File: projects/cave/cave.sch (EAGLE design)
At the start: 113 parts, among them U1 IRLML6344TRPBF, U10 IRLML6344TRPBF, U11 IRLML6344TRPBF, U12 IRLML6344TRPBF, U2 TLC555CDR, U3 IRLML6344TRPBF, U4 IRLML6344TRPBF, U5 IRLML6344TRPBF, U6 IRLML6344TRPBF, U7 TPS54625, U9 IRLML6344TRPBF

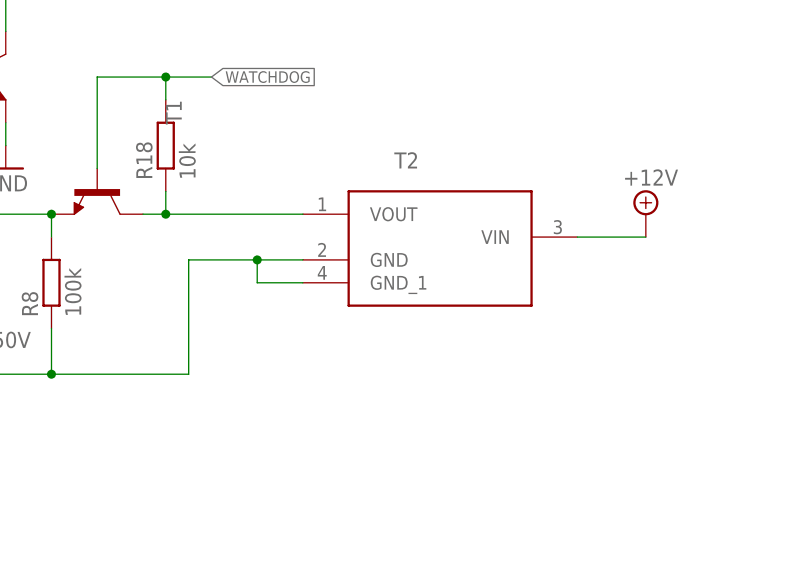
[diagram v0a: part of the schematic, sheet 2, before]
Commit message: Board dimension reduced to 99x70mm (Seeed's limitations). Gerber revA generated
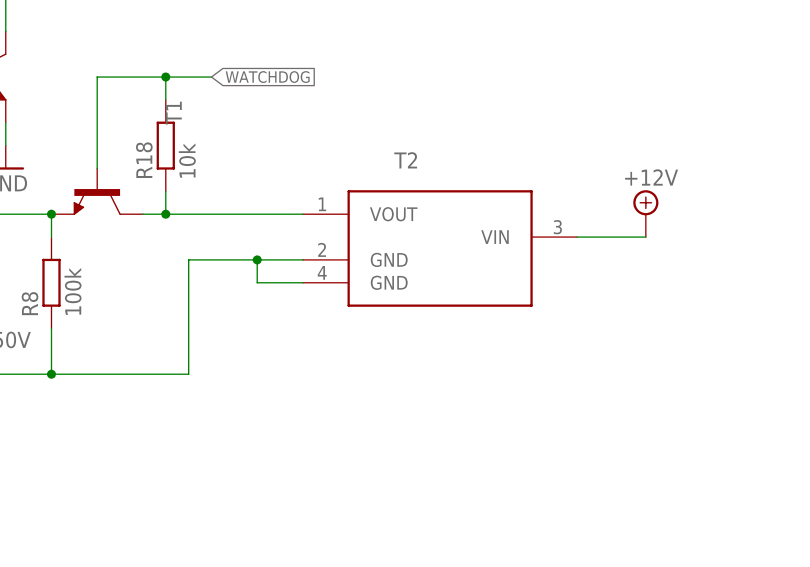
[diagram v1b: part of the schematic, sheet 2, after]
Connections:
- net GND: now also T2.GND@1, T2.GND@2; no longer T2.GND, T2.GND_1
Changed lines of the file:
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@@
 <wire x1="139.7" y1="-25.4" x2="121.92" y2="-25.4" width="0.1524" layer="91"/>
 <junction x="121.92" y="-25.4"/>
-<pinref part="T2" gate="A" pin="GND"/>
+<pinref part="T2" gate="A" pin="GND@1"/>
 <wire x1="167.64" y1="-12.7" x2="162.56" y2="-12.7" width="0.1524" layer="91"/>
 <wire x1="162.56" y1="-12.7" x2="154.94" y2="-12.7" width="0.1524" layer="91"/>
@@
 <wire x1="154.94" y1="-25.4" x2="139.7" y2="-25.4" width="0.1524" layer="91"/>
 <junction x="139.7" y="-25.4"/>
-<pinref part="T2" gate="A" pin="GND_1"/>
+<pinref part="T2" gate="A" pin="GND@2"/>
 <wire x1="167.64" y1="-15.24" x2="162.56" y2="-15.24" width="0.1524" layer="91"/>
 <wire x1="162.56" y1="-15.24" x2="162.56" y2="-12.7" width="0.1524" layer="91"/>

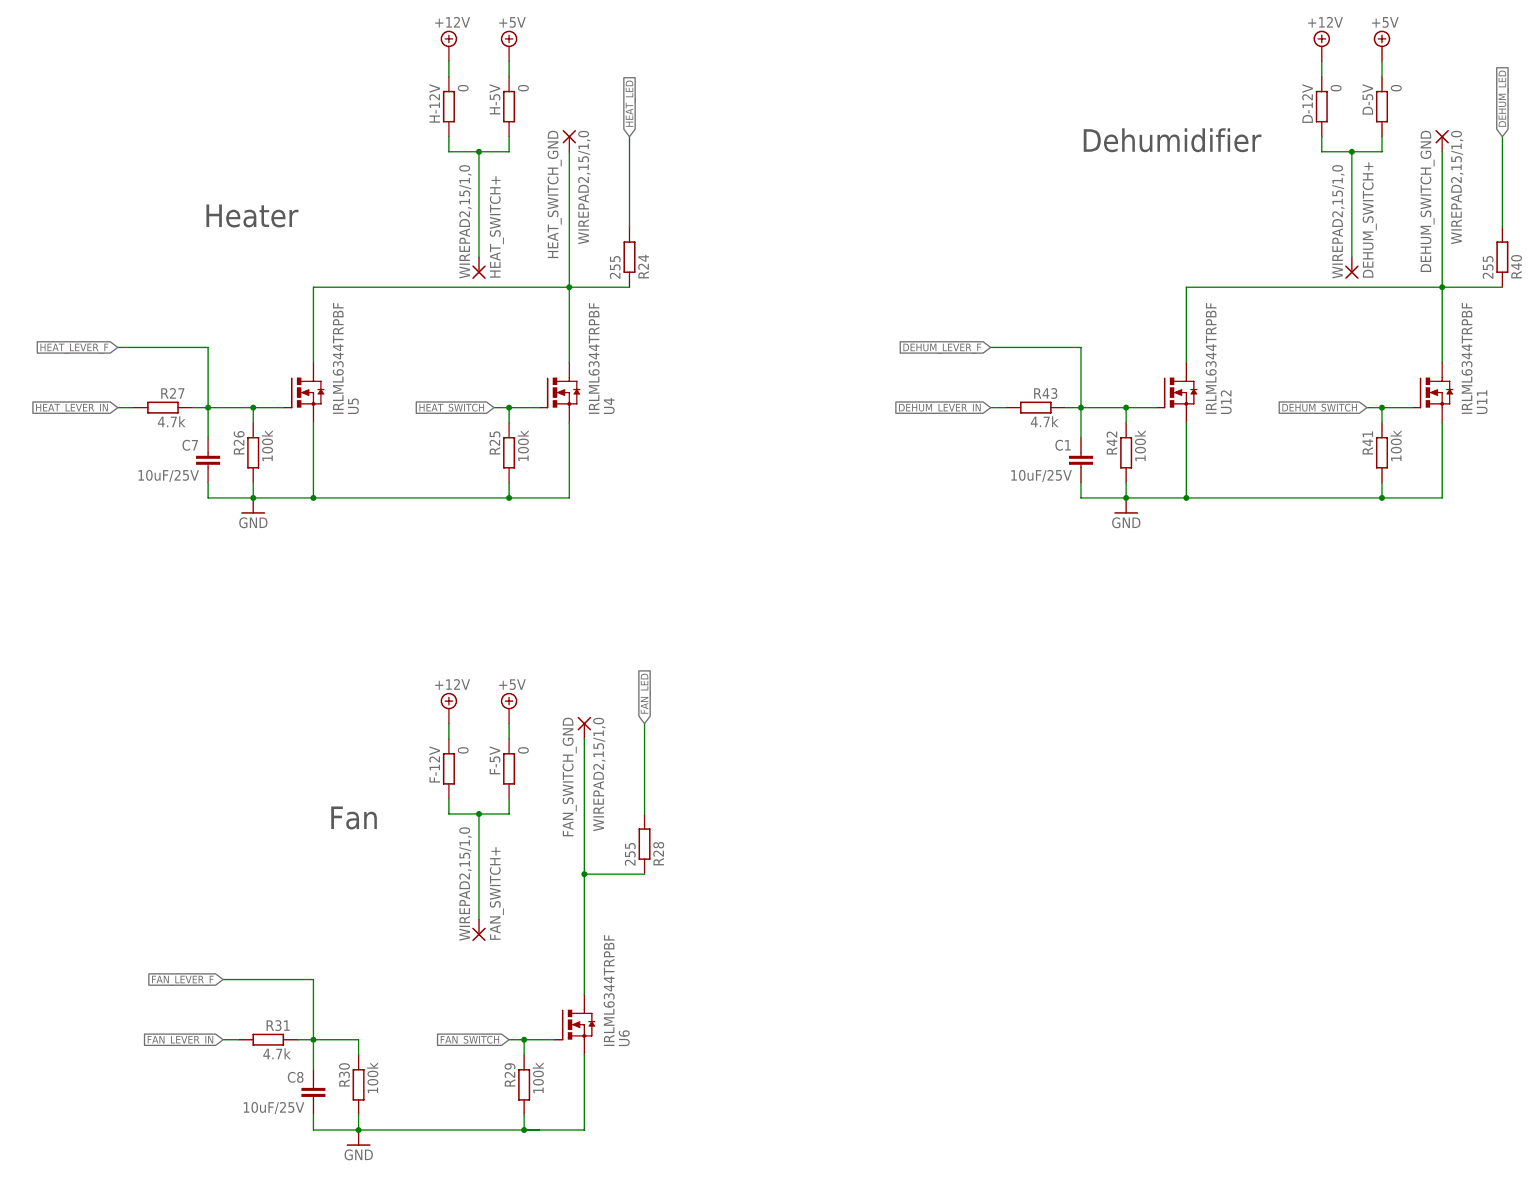
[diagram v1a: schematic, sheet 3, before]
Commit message: Added free wheel diode between the relays' terminal.
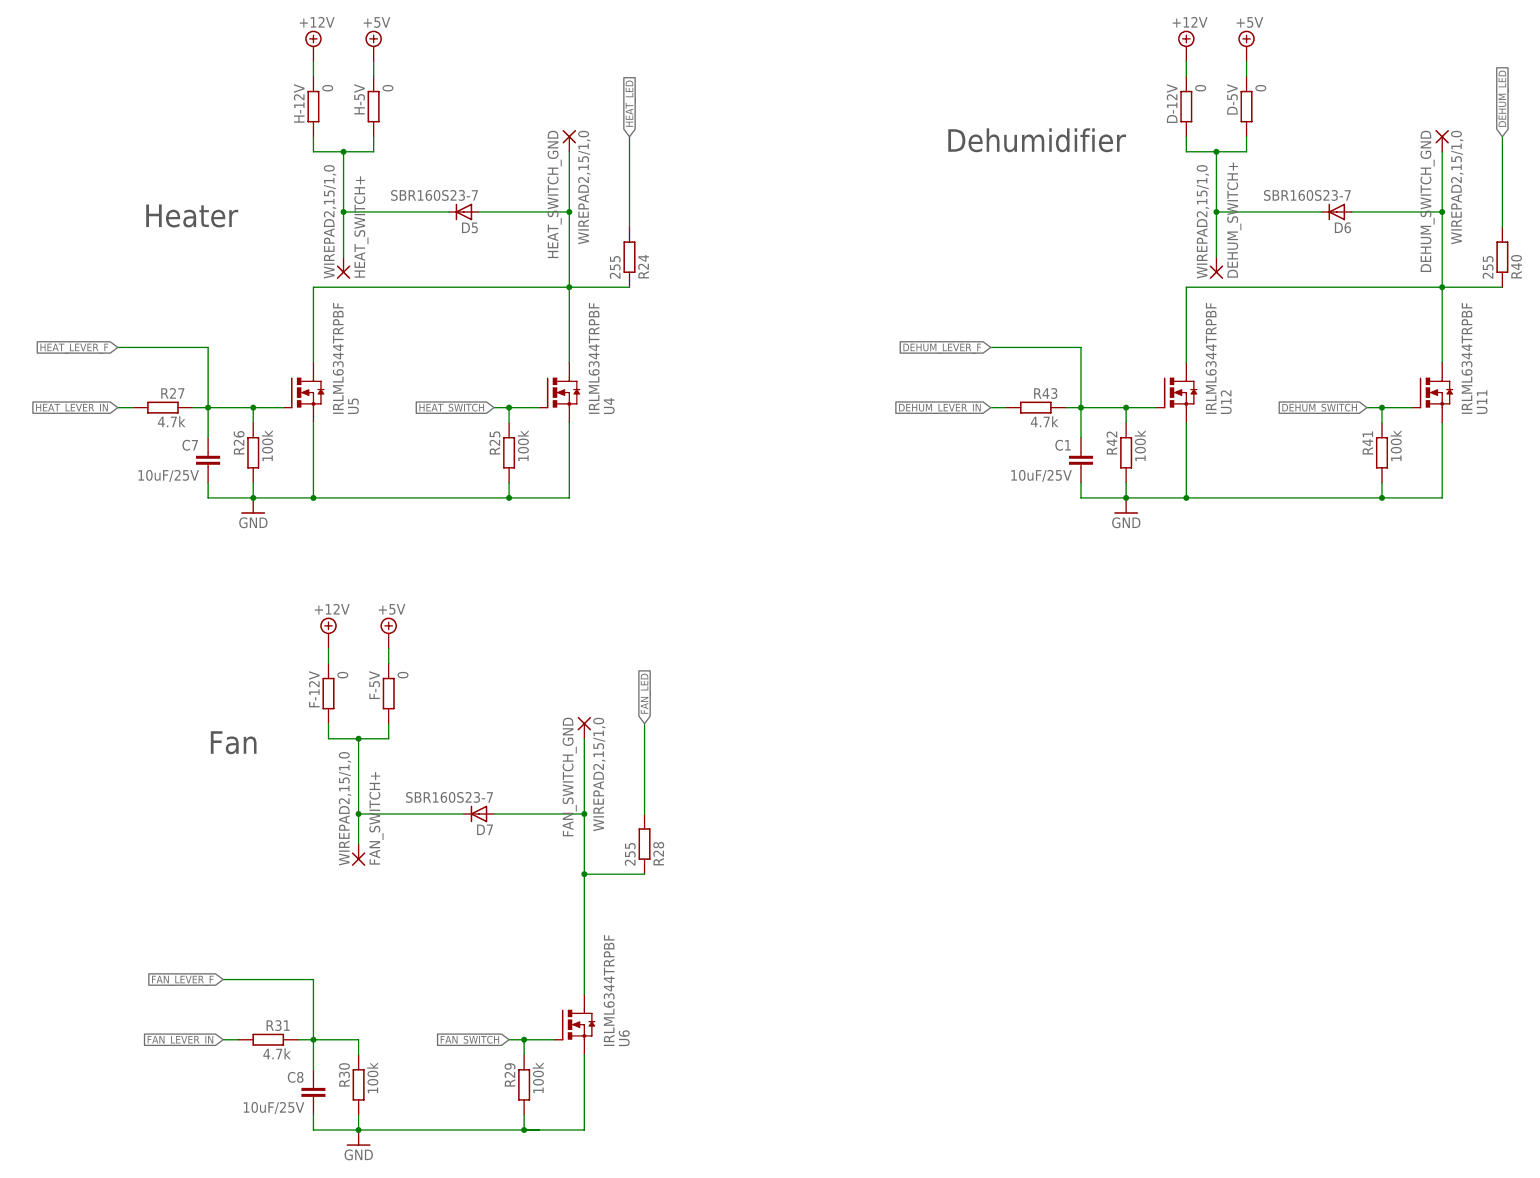
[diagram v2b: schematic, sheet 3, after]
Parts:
- added D5, D6, D7: SBR160S23-7, semicon-smd-ipc:D-A1-C3
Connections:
- removed net N$21: HEAT_SWITCH_GND.P, R24.1, U4.D, U5.D
- removed net N$23: FAN_SWITCH_GND.P, R28.1, U6.D
- removed net N$24: DEHUM_SWITCH_GND.P, R40.1, U11.D, U12.D
- new net +12V1: D5.A, HEAT_SWITCH_GND.P, R24.1, U4.D, U5.D
- new net +12V2: D6.A, DEHUM_SWITCH_GND.P, R40.1, U11.D, U12.D
- new net +12V3: D7.A, FAN_SWITCH_GND.P, R28.1, U6.D
- net N$22: now also D7.C
- net N$26: now also D5.C
- net N$27: now also D6.C
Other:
- moved on the sheet: D-12V, D-5V, DEHUM_SWITCH+, F-12V, F-5V, FAN_SWITCH+, H-12V, H-5V, HEAT_SWITCH+

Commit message: Fixed silkscreen error on top-board wirepads (forgot to update it after a81e98b). Changed some ill-named-nets' names for relays' GND.
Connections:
- net +12V1 renamed HEAT_GND
- net +12V2 renamed DEHUM_GND
- net +12V3 renamed FAN_GND
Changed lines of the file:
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@@
 </segment>
 </net>
-<net name="+12V1" class="0">
+<net name="HEAT_GND" class="0">
 <segment>
 <pinref part="D5" gate="G$1" pin="A"/>
@@
 </segment>
 </net>
-<net name="+12V2" class="0">
+<net name="DEHUM_GND" class="0">
 <segment>
 <pinref part="D6" gate="G$1" pin="A"/>
@@
 </segment>
 </net>
-<net name="+12V3" class="0">
+<net name="FAN_GND" class="0">
 <segment>
 <pinref part="D7" gate="G$1" pin="A"/>

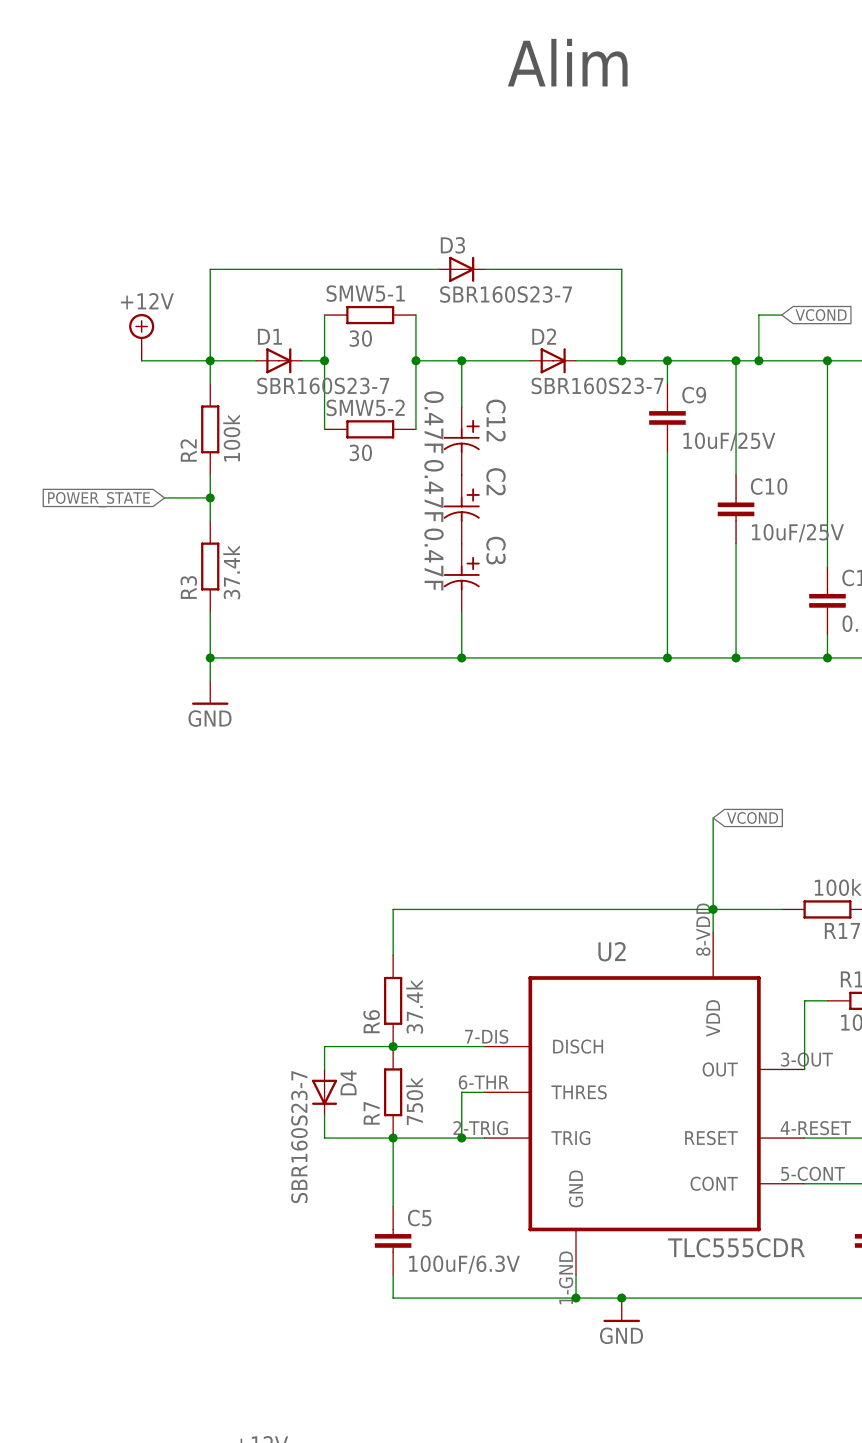
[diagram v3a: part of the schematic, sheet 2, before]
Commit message: MAJOR MODIFICATIONS: Changed power capacitor : previous ones didn't sustain discharge current Changed 555 capacitor : previous one was at 6.3V max (instead of 12V), AND not accurate enough -> switch to tantale capa Modified light_sensor circuit to use a phototransistor. The potentiometer is for schematic purpose, the package is NOT right !
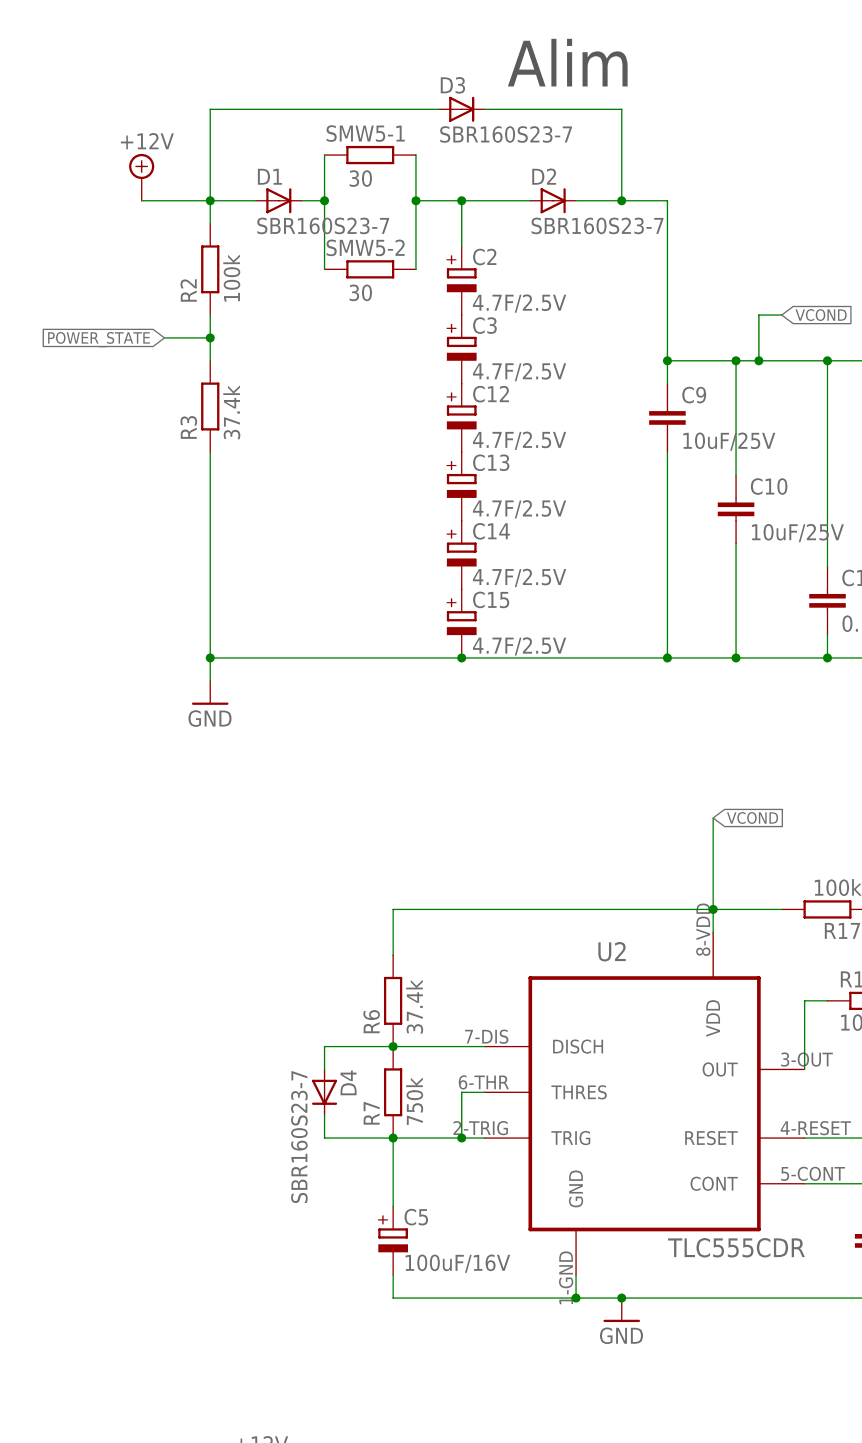
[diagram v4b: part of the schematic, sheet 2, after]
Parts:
- removed LIGHTSEN_GND: WIREPAD2,15/1,0, wirepad:WIREPAD2,15/1,0
- added C13, C14, C15: 4.7F/2.5V, rcl:CPOL-EUE5-10.5
- added C16: 0.1uF/25V, rcl:C-EUC0603
- added R12: 5k, rcl:POTENTIOMETER_PT_SPIN
- added R4: 100, rcl:R-EU_R0603
- C12, C2, C3: value 0.47F -> 4.7F/2.5V; device Panasonic-EEC-EECR-EECF-EECS:EECF5R5U474-D21.5 -> rcl:CPOL-EUE5-10.5
- C5: value 100uF/6.3V -> 100uF/16V; device rcl:C-EUC0805 -> resistor:CPOL-EUD/7343-31W
- R1, R11, R16, R25, R26, R29, R30, R39, R41, R42: value 100k -> 10k
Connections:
- new net N$18: C13.-, C14.+
- new net N$19: C14.-, C15.+
- new net N$21: C16.1, LIGHTSEN_SIG.P, R12.2, R4.2
- new net N$8: C12.-, C13.+
- net +3V3: now also LIGHTSEN_5V.P
- net +5V: no longer LIGHTSEN_5V.P
- net GND: now also C15.-, C16.2, C5.-, R12.3; no longer C3.2, C5.2, LIGHTSEN_GND.P
- net LIGHT_SENSOR: now also R4.1; no longer LIGHTSEN_SIG.P
- net N$1: now also C2.+; no longer C12.1
- net N$2: now also C2.-, C3.+; no longer C12.2, C2.1
- net N$3: now also C12.+, C3.-; no longer C2.2, C3.1
- net N$6: now also C5.+; no longer C5.1
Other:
- moved on the sheet: D1, D2, D3, R2, R3, SMW5-1, SMW5-2

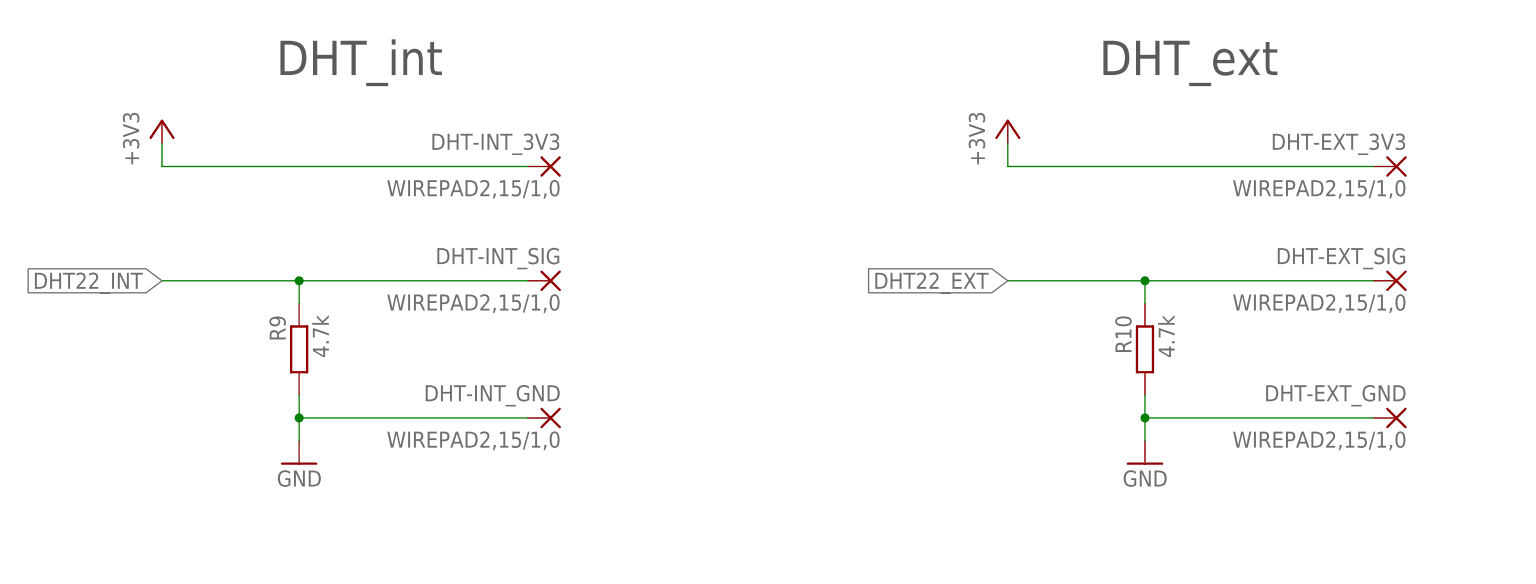
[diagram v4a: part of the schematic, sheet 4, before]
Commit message: DHT22 circuit : the 4.7kOhm resistor change to pullup instead of pulldown (pulldown NOT working). Now DHT22 readings work fine.
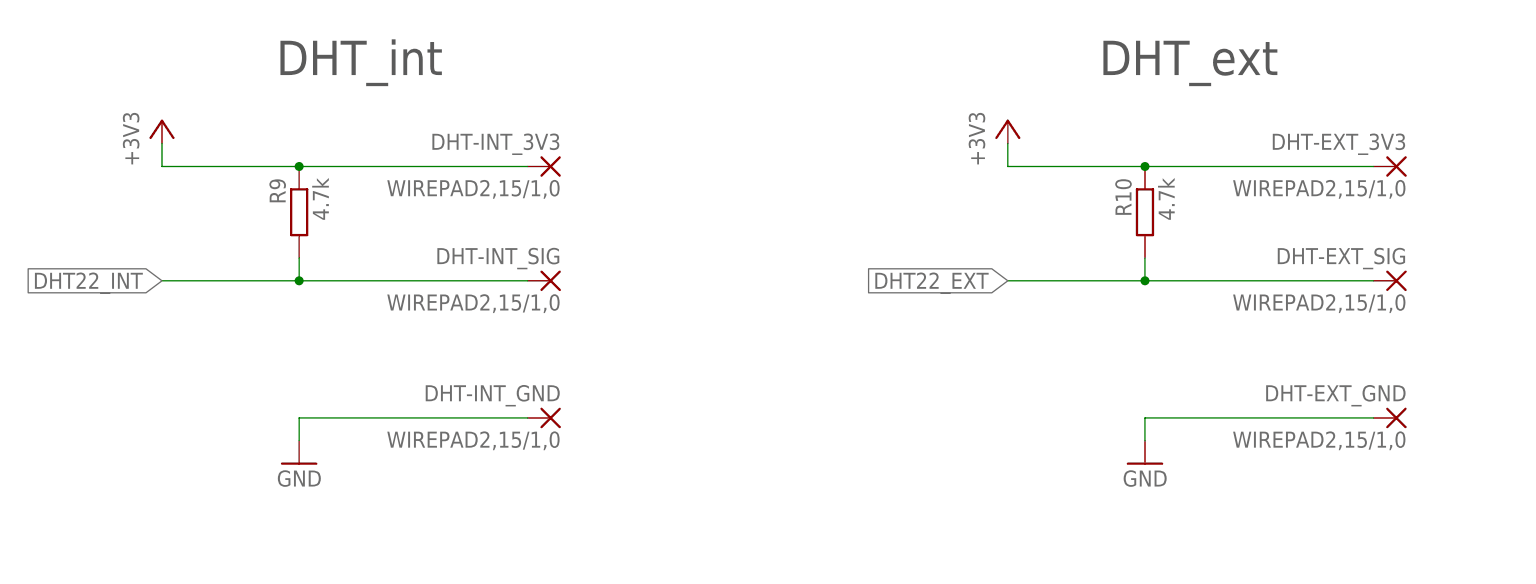
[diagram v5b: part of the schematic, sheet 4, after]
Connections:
- net +3V3: now also R10.1, R9.1
- net DHT22_EXT: now also R10.2; no longer R10.1
- net DHT22_INT: now also R9.2; no longer R9.1
- net GND: no longer R10.2, R9.2
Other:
- moved on the sheet: R10, R9
